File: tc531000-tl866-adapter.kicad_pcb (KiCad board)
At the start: 2 copper layers, 56.4 x 36.1 mm, 9 parts, among them U1 TC531000, U2 27C010

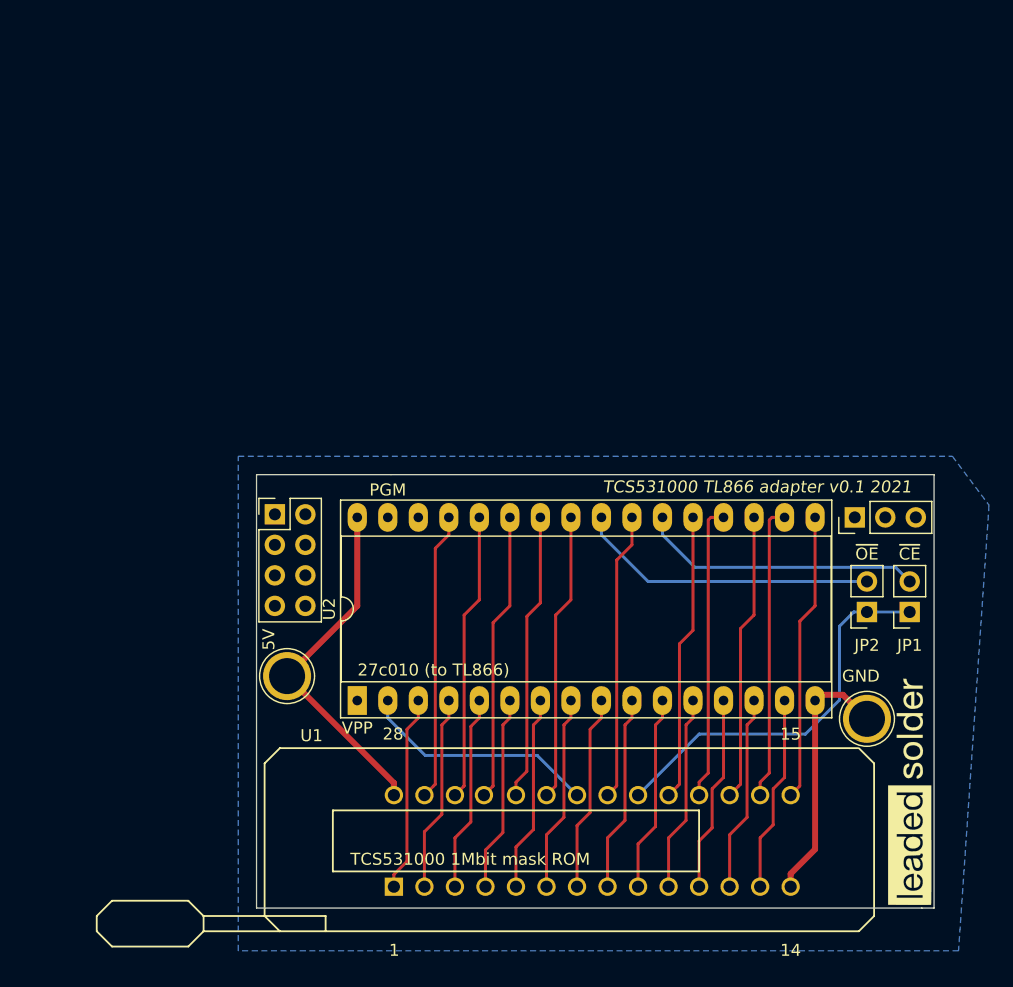
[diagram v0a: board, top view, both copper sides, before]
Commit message: Mini version but overhang is on the wrong side
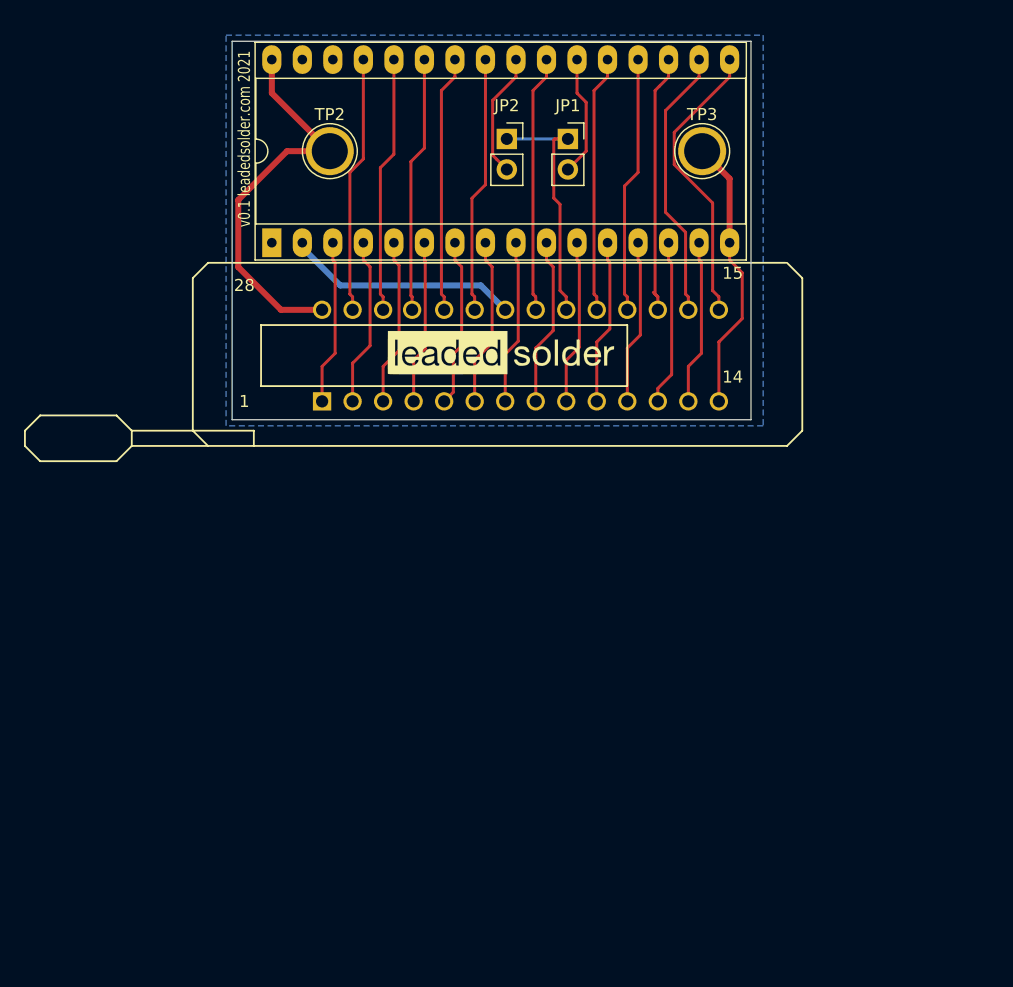
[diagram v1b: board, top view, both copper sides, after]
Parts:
- removed REF**: PinHeader_1x03_P2.54mm_Vertical, Connector_PinHeader_2.54mm:PinHeader_1x03_P2.54mm_Vertical
- removed REF**: PinHeader_2x04_P2.54mm_Vertical, Connector_PinHeader_2.54mm:PinHeader_2x04_P2.54mm_Vertical
- moved G*** 50.0 mm to (129.0, 51.8), turned to 0 degrees
- moved JP2 49.5 mm to (129.5, 34.0), turned to 0 degrees
- moved TP3 49.2 mm to (145.8, 35.1)
- moved JP1 48.6 mm to (134.6, 34.0), turned to 0 degrees
- moved TP2 43.8 mm to (114.8, 35.1)
- moved U1 40.8 mm to (125.6, 52.1)
- moved U2 38.8 mm to (110.0, 42.7)
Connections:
- net Net-(U1-Pad22) renamed /a16
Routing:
- net /~OE: track 25.2 -> 10.4 mm
- net /~CE: track 23.6 -> 10.1 mm
- net /~TOSHIBA_CE: track 32.5 -> 20.9 mm
- net /5V: track 29.2 -> 33.0 mm
- net Net-(U1-Pad18): track 24.6 -> 21.4 mm
- net Net-(U1-Pad4): track 16.3 -> 13.6 mm
- net Net-(U1-Pad25): track 24.0 -> 21.3 mm
- net Net-(U1-Pad11): track 16.3 -> 13.7 mm
- net Net-(U1-Pad1): track 16.3 -> 13.7 mm
- net Net-(U1-Pad10): track 16.3 -> 13.7 mm
- net Net-(U1-Pad9): track 16.3 -> 13.7 mm
- net Net-(U1-Pad7): track 16.3 -> 13.7 mm
- net Net-(U1-Pad13): track 16.3 -> 13.7 mm
- net Net-(U1-Pad26): track 24.0 -> 21.4 mm
- net Net-(U1-Pad24): track 24.0 -> 21.4 mm
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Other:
- board size 56.4 x 36.1 mm -> 43.2 x 31.5 mm
- board text added: "27c010"
- board text added: "a16"
- board text added: "tcs531000"
- board text added: "v0.1 leadedsolder.com 2021"
- board text added: "vtech just kicked in, yo"
- board text removed: "27c010 (to TL866)"
- board text removed: "PGM"
- board text removed: "TCS531000 1Mbit mask ROM"
- board text removed: "TCS531000 TL866 adapter v0.1 2021"
- board text removed: "VPP"
- board text removed: "call your mom"
- board text removed: "leadedsolder.com"
- board text removed: "man this 1mbit rom is pretty big isn't it"

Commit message: V0.1 sent to osh
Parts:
- moved TP3 39.3 mm to (110.7, 52.8)
- moved U2 36.9 mm to (146.8, 44.7), turned to 270 degrees
- moved TP2 33.1 mm to (142.7, 52.8)
- moved JP1 21.6 mm to (124.0, 52.8), turned to 270 degrees
- moved JP2 18.9 mm to (131.6, 52.8), turned to 270 degrees
- moved U1 18.4 mm to (131.1, 69.6), turned to 180 degrees
- moved G*** 3.87 mm to (127.5, 48.3)
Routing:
- net /a16: track 19.4 -> 45.6 mm
- net /~TOSHIBA_CE: track 20.9 -> 45.7 mm
- net Net-(U1-Pad15): track 24.3 -> 14.0 mm
- net Net-(U1-Pad1): track 13.7 -> 23.5 mm
- net Net-(U1-Pad9): track 13.7 -> 22.9 mm
- net /5V: track 33.0 -> 24.0 mm
- net Net-(U1-Pad16): track 22.8 -> 14.0 mm
- net Net-(U1-Pad13): track 13.7 -> 22.3 mm
- net Net-(U1-Pad8): track 14.0 -> 22.4 mm
- net Net-(U1-Pad11): track 13.7 -> 21.9 mm
- net Net-(U1-Pad12): track 13.8 -> 21.9 mm
- net Net-(U1-Pad4): track 13.6 -> 21.7 mm
- net Net-(U1-Pad10): track 13.7 -> 21.7 mm
- net Net-(U1-Pad7): track 13.7 -> 21.7 mm
- net Net-(U1-Pad17): track 21.9 -> 14.0 mm
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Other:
- board size 43.2 x 31.5 mm -> 41.7 x 32 mm
- board text added: "pin 1"
- board text added: "tc531000 tl866 adapter"
- board text added: "v0.1, leadedsolder.com 2021"
- board text removed: "v0.1 leadedsolder.com 2021"
- board text removed: "vtech just kicked in, yo"

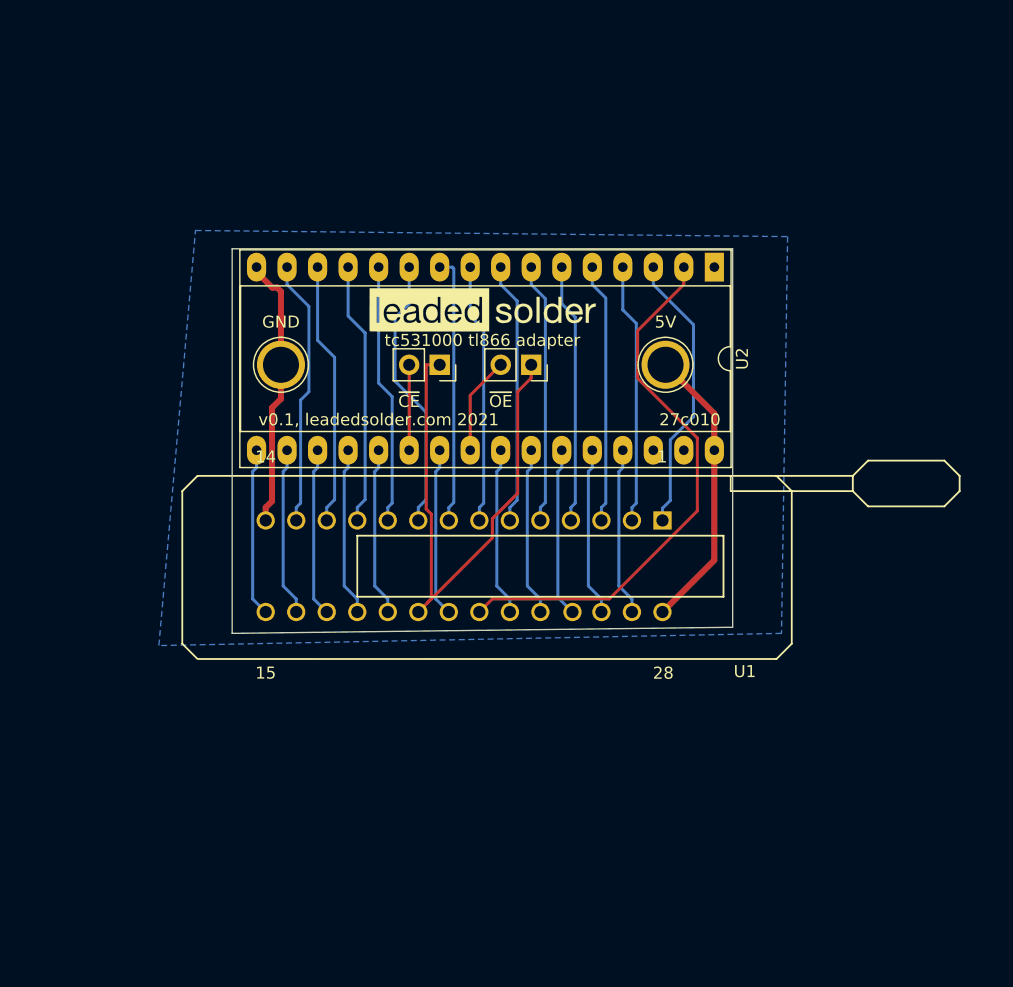
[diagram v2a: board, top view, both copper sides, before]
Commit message: Use a standard 28 pin DIP socket with some extra space around it. Wait for the ZIF to see if it fits
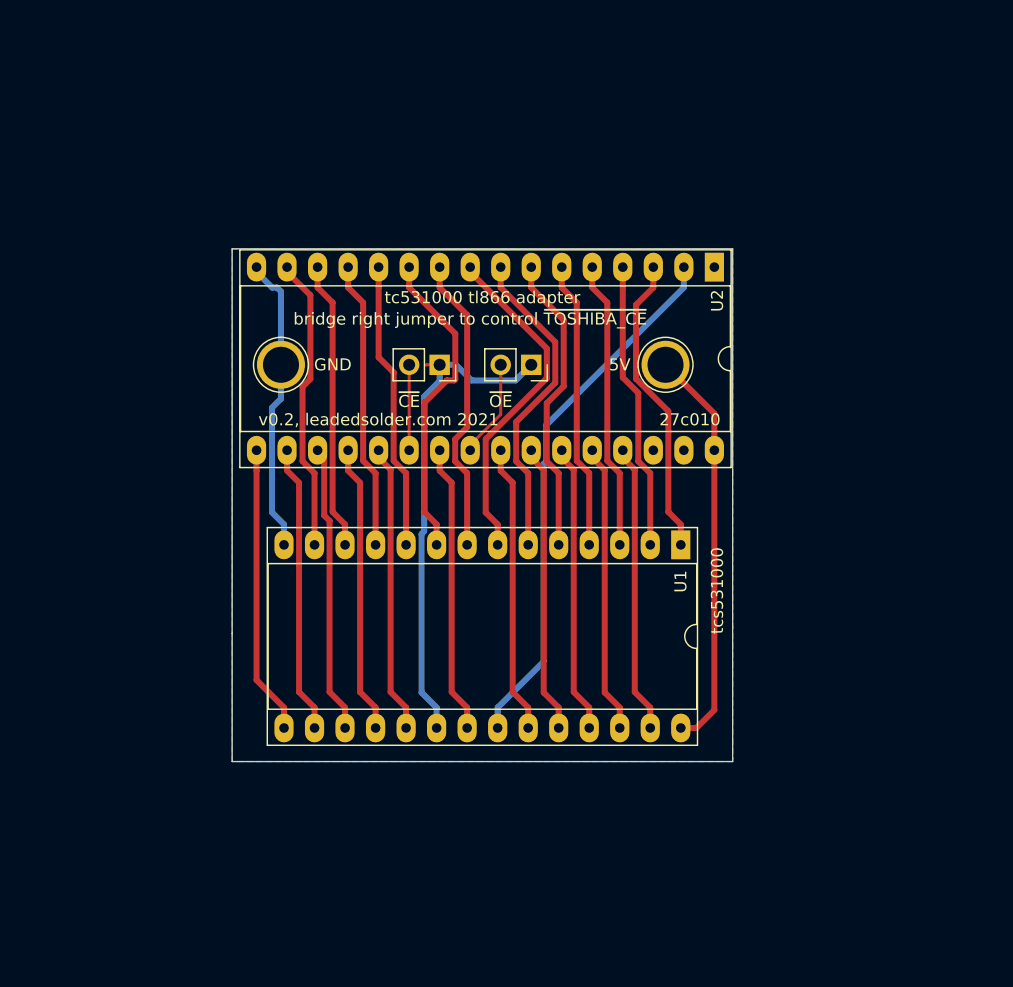
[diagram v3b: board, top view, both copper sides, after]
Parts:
- removed G***: LOGO, logos:leaded-solder-logo-800dpi
- U1: footprint kicad_zif socket:228-3341 -> Package_DIP:DIP-28_W15.24mm_Socket_LongPads
- moved U1 13.1 mm to (144.0, 67.8), turned to 270 degrees
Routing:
- net Net-(U1-Pad17): track 14.0 -> 24.1 mm
- net Net-(U1-Pad26): track 14.0 -> 24.1 mm
- net Net-(U1-Pad21): track 14.0 -> 24.1 mm
- net Net-(U1-Pad19): track 14.0 -> 24.1 mm
- net Net-(U1-Pad18): track 14.0 -> 24.1 mm
- net Net-(U1-Pad16): track 14.0 -> 24.1 mm
- net Net-(U1-Pad15): track 14.0 -> 24.1 mm
- net Net-(U1-Pad24): track 14.0 -> 24.1 mm
- net Net-(U1-Pad27): track 14.0 -> 24.1 mm
- net Net-(U1-Pad23): track 14.0 -> 24.1 mm
- net Net-(U1-Pad25): track 14.1 -> 24.1 mm
- net /5V: track 24.0 -> 33.8 mm
- net Net-(U1-Pad7): track 21.7 -> 28.3 mm
- net Net-(U1-Pad6): track 21.9 -> 26.8 mm
- net /~TOSHIBA_CE: track 45.7 -> 41.2 mm
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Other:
- board size 41.7 x 32 mm -> 41.7 x 42.7 mm
- board text added: "bridge right jumper to control ~TOSHIBA_CE"
- board text added: "v0.2, leadedsolder.com 2021"
- board text removed: "v0.1, leadedsolder.com 2021"

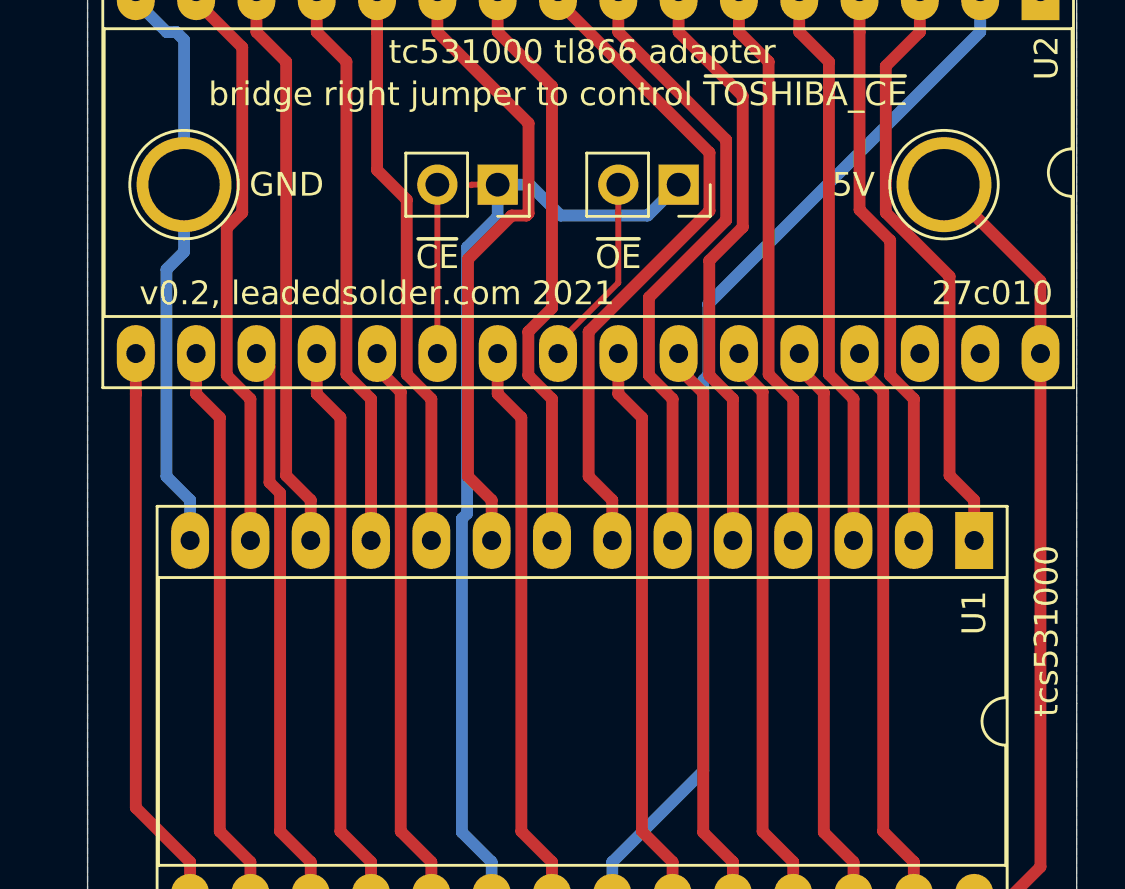
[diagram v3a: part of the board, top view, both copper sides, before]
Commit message: Fix file for KiCad 7
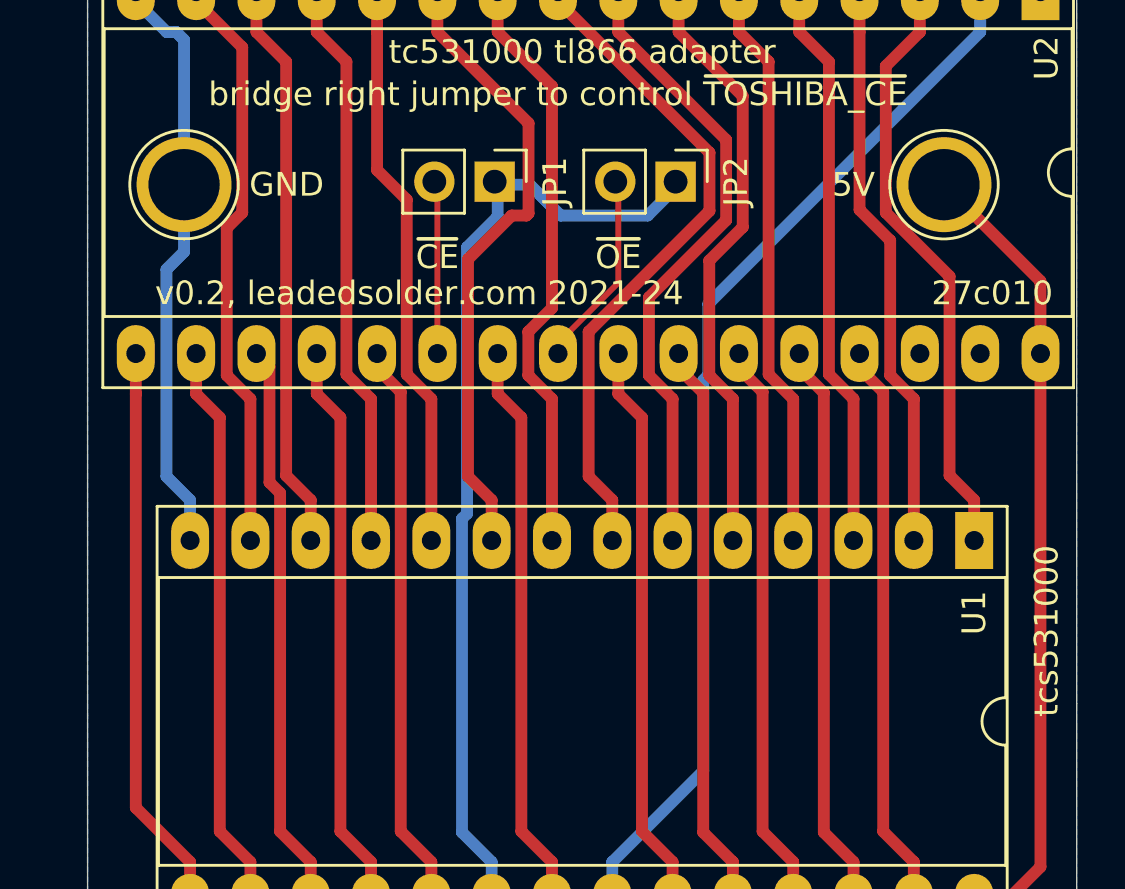
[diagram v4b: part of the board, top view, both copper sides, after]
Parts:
- JP1, JP2: value Jumper_NO_Small -> Jumper_2_Bridged; footprint Connector_PinSocket_2.54mm:PinSocket_1x02_P2.54mm_Vertical -> Connector_PinHeader_2.54mm:PinHeader_1x02_P2.54mm_Vertical
- moved JP2 0.18 mm to (131.4, 52.7)
- moved JP1 0.18 mm to (123.8, 52.7)
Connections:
- net /~CE renamed /~{CE}
- net /~OE renamed /~{OE}
- net /~TOSHIBA_CE renamed /~{TOSHIBA_CE}
- U2 pad 1: Net-(U2-Pad1) -> unconnected-(U2-VPP-Pad1)
- U2 pad 31: Net-(U2-Pad31) -> unconnected-(U2-~{PGM}-Pad31)
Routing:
- net /~{TOSHIBA_CE}: track 41.2 -> 40.1 mm
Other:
- net class Default removed
- board text added: "bridge right jumper to control ~{TOSHIBA_CE}"
- board text added: "v0.2, leadedsolder.com 2021-24"
- board text added: "~{CE}"
- board text added: "~{OE}"
- board text removed: "bridge right jumper to control ~TOSHIBA_CE"
- board text removed: "v0.2, leadedsolder.com 2021"
- board text removed: "~CE"
- board text removed: "~OE"
